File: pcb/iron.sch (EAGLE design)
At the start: 22 parts, among them IC1 AT24CS04-SOT23, IC2 TS507CLT, IC3 AD7995, IC4 ESDA6V1SC5, X1 LUMBERG_KLB_4

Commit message: reworked iron parts
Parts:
- C1: OC_DIGIKEY (none) -> 478-7926-1-ND; OC_MOUSER 710-885012207080 -> (none)
- C2: OC_DIGIKEY (none) -> 478-6209-1-ND; OC_MOUSER 710-885012207092 -> (none)
- R1: value 20k 0,1% -> 1k; OC_DIGIKEY P20KDBCT-ND -> P1.0KDBCT-ND
- R2: value 68k @25°C, 1%, ß=3985 K -> 1k @25°C, 1%, ß=3650 K; OC_DIGIKEY BC2555CT-ND -> P123687CT-ND
- R4: value 5,1M -> 4M7; OC_DIGIKEY (none) -> 311-4.70MHRCT-ND; OC_MOUSER 71-CRCW08055M10FKEA -> (none)
- R6: value 1k -> 100k; OC_DIGIKEY RMCF0603FT1K00CT-ND -> RMCF0603FT100KCT-ND
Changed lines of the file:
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@@
 <part name="X1" library="solderpi" library_urn="urn:adsk.eagle:library:1437534" deviceset="LUMBERG_KLB_4" device="" package3d_urn="urn:adsk.eagle:package:1437574/2"/>
 <part name="GND1" library="supply1" library_urn="urn:adsk.eagle:library:371" deviceset="GND" device=""/>
-<part name="R1" library="common" library_urn="urn:adsk.eagle:library:8241912" deviceset="R-EU" device="0603" package3d_urn="urn:adsk.eagle:package:8241925/3" value="20k 0,1%">
-<spice>
-<pinmapping spiceprefix="R">
-<pinmap gate="G$1" pin="1" pinorder="1"/>
-<pinmap gate="G$1" pin="2" pinorder="2"/>
-</pinmapping>
-</spice>
-<attribute name="OC_DIGIKEY" value="P20KDBCT-ND"/>
-</part>
-<part name="R2" library="common" library_urn="urn:adsk.eagle:library:8241912" deviceset="NTC" device="0603" package3d_urn="urn:adsk.eagle:package:8241925/3" value="68k @25°C, 1%, ß=3985 K">
-<attribute name="OC_DIGIKEY" value="BC2555CT-ND"/>
+<part name="R1" library="common" library_urn="urn:adsk.eagle:library:8241912" deviceset="R-EU" device="0603" package3d_urn="urn:adsk.eagle:package:8241925/3" value="1k">
+<spice>
+<pinmapping spiceprefix="R">
+<pinmap gate="G$1" pin="1" pinorder="1"/>
+<pinmap gate="G$1" pin="2" pinorder="2"/>
+</pinmapping>
+</spice>
+<attribute name="OC_DIGIKEY" value="P1.0KDBCT-ND"/>
+</part>
+<part name="R2" library="common" library_urn="urn:adsk.eagle:library:8241912" deviceset="NTC" device="0603" package3d_urn="urn:adsk.eagle:package:8241925/3" value="1k @25°C, 1%, ß=3650 K">
+<attribute name="OC_DIGIKEY" value="P123687CT-ND"/>
 </part>
 <part name="P+1" library="supply1" library_urn="urn:adsk.eagle:library:371" deviceset="+5V" device=""/>
@@
 <part name="GND4" library="supply1" library_urn="urn:adsk.eagle:library:371" deviceset="GND" device=""/>
 <part name="P+2" library="supply1" library_urn="urn:adsk.eagle:library:371" deviceset="+5V" device=""/>
-<part name="R4" library="common" library_urn="urn:adsk.eagle:library:8241912" deviceset="R-EU" device="0603" package3d_urn="urn:adsk.eagle:package:8241925/3" value="5,1M">
-<spice>
-<pinmapping spiceprefix="R">
-<pinmap gate="G$1" pin="1" pinorder="1"/>
-<pinmap gate="G$1" pin="2" pinorder="2"/>
-</pinmapping>
-</spice>
-<attribute name="OC_MOUSER" value="71-CRCW08055M10FKEA"/>
+<part name="R4" library="common" library_urn="urn:adsk.eagle:library:8241912" deviceset="R-EU" device="0603" package3d_urn="urn:adsk.eagle:package:8241925/3" value="4M7">
+<spice>
+<pinmapping spiceprefix="R">
+<pinmap gate="G$1" pin="1" pinorder="1"/>
+<pinmap gate="G$1" pin="2" pinorder="2"/>
+</pinmapping>
+</spice>
+<attribute name="OC_DIGIKEY" value="311-4.70MHRCT-ND"/>
 </part>
 <part name="R5" library="common" library_urn="urn:adsk.eagle:library:8241912" deviceset="R-EU" device="0603" package3d_urn="urn:adsk.eagle:package:8241925/3" value="1k">
@@
 <attribute name="OC_DIGIKEY" value=" RMCF0603FT1K00CT-ND"/>
 </part>
-<part name="R6" library="common" library_urn="urn:adsk.eagle:library:8241912" deviceset="R-EU" device="0603" package3d_urn="urn:adsk.eagle:package:8241925/3" value="1k">
-<spice>
-<pinmapping spiceprefix="R">
-<pinmap gate="G$1" pin="1" pinorder="1"/>
-<pinmap gate="G$1" pin="2" pinorder="2"/>
-</pinmapping>
-</spice>
-<attribute name="OC_DIGIKEY" value=" RMCF0603FT1K00CT-ND"/>
+<part name="R6" library="common" library_urn="urn:adsk.eagle:library:8241912" deviceset="R-EU" device="0603" package3d_urn="urn:adsk.eagle:package:8241925/3" value="100k">
+<spice>
+<pinmapping spiceprefix="R">
+<pinmap gate="G$1" pin="1" pinorder="1"/>
+<pinmap gate="G$1" pin="2" pinorder="2"/>
+</pinmapping>
+</spice>
+<attribute name="OC_DIGIKEY" value="RMCF0603FT100KCT-ND"/>
 </part>
 <part name="C1" library="common" library_urn="urn:adsk.eagle:library:8241912" deviceset="C-EU" device="0603" package3d_urn="urn:adsk.eagle:package:8241929/3" value="100pF">
@@
 </pinmapping>
 </spice>
-<attribute name="OC_MOUSER" value="710-885012207080"/>
+<attribute name="OC_DIGIKEY" value="478-7926-1-ND"/>
 </part>
 <part name="C2" library="common" library_urn="urn:adsk.eagle:library:8241912" deviceset="C-EU" device="0603" package3d_urn="urn:adsk.eagle:package:8241929/3" value="10nF">
@@
 </pinmapping>
 </spice>
-<attribute name="OC_MOUSER" value="710-885012207092 "/>
+<attribute name="OC_DIGIKEY" value="478-6209-1-ND"/>
 </part>
 <part name="P+3" library="supply1" library_urn="urn:adsk.eagle:library:371" deviceset="+5V" device=""/>
@@
 </instance>
 <instance part="R4" gate="G$1" x="22.86" y="66.04" smashed="yes" rot="R90">
-<attribute name="OC_MOUSER" x="22.86" y="66.04" size="1.778" layer="96" rot="R90" display="off"/>
+<attribute name="OC_DIGIKEY" x="22.86" y="66.04" size="1.778" layer="96" rot="R90" display="off"/>
 <attribute name="NAME" x="21.3614" y="62.23" size="1.778" layer="95" rot="R90"/>
 <attribute name="VALUE" x="26.162" y="62.23" size="1.778" layer="96" rot="R90"/>
@@
 </instance>
 <instance part="C1" gate="G$1" x="12.7" y="63.5" smashed="yes">
-<attribute name="OC_MOUSER" x="12.7" y="63.5" size="1.778" layer="96" display="off"/>
+<attribute name="OC_DIGIKEY" x="12.7" y="63.5" size="1.778" layer="96" display="off"/>
 <attribute name="NAME" x="14.224" y="63.881" size="1.778" layer="95"/>
 <attribute name="VALUE" x="14.224" y="58.801" size="1.778" layer="96"/>
 </instance>
 <instance part="C2" gate="G$1" x="60.96" y="111.76" smashed="yes">
-<attribute name="OC_MOUSER" x="60.96" y="111.76" size="1.778" layer="96" display="off"/>
+<attribute name="OC_DIGIKEY" x="60.96" y="111.76" size="1.778" layer="96" display="off"/>
 <attribute name="NAME" x="62.484" y="112.141" size="1.778" layer="95"/>
 <attribute name="VALUE" x="62.484" y="107.061" size="1.778" layer="96"/>

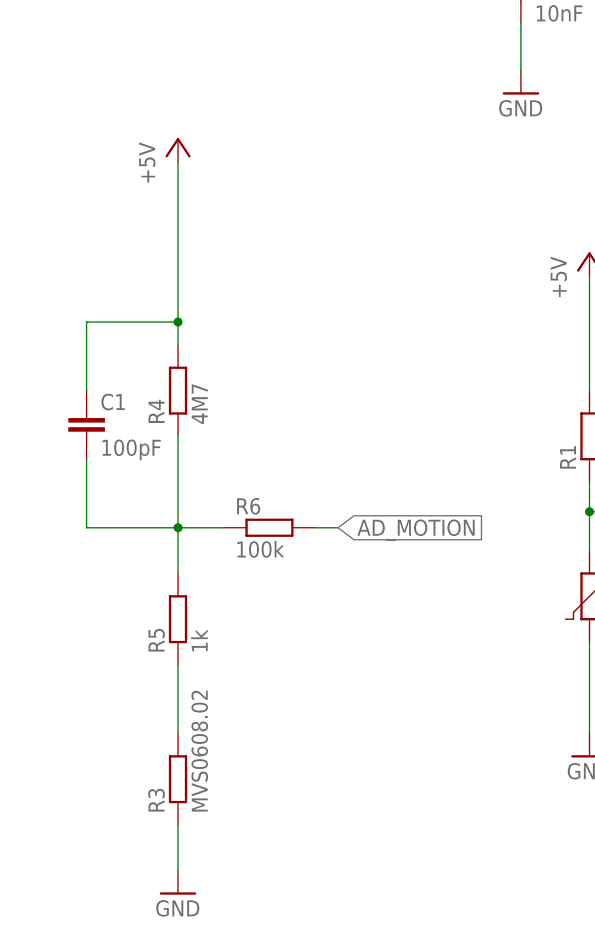
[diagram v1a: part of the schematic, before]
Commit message: shottky diode added to iron/tweezer
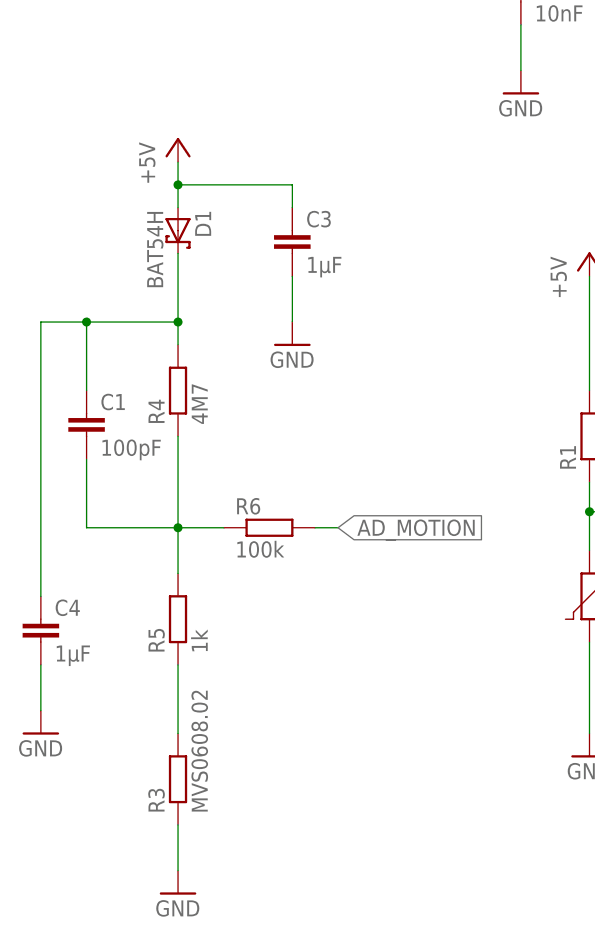
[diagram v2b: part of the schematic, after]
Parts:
- added C3, C4: 1µF, common:C-EU0603
- added D1: BAT54H, solderpi:BAT54H
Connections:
- new net N$1: C1.1, C4.1, D1.C, R4.2
- net +5V: now also C3.1, D1.A; no longer C1.1, R4.2
- net GND: now also C3.2, C4.2
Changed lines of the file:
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@@
 <attribute name="OC_DIGIKEY" value="YAG4498CT-ND"/>
 </part>
+<part name="D1" library="solderpi" library_urn="urn:adsk.eagle:library:1437534" deviceset="BAT54H" device="" package3d_urn="urn:adsk.eagle:package:1609183/2">
+<attribute name="OC_DIGIKEY" value="1727-3569-1-ND"/>
+</part>
+<part name="C3" library="common" library_urn="urn:adsk.eagle:library:8241912" deviceset="C-EU" device="0603" package3d_urn="urn:adsk.eagle:package:8241929/3" value="1µF">
+<spice>
+<pinmapping spiceprefix="C">
+<pinmap gate="G$1" pin="1" pinorder="1"/>
+<pinmap gate="G$1" pin="2" pinorder="2"/>
+</pinmapping>
+</spice>
+<attribute name="OC_DIGIKEY" value="1276-1034-1-ND"/>
+</part>
+<part name="GND11" library="supply1" library_urn="urn:adsk.eagle:library:371" deviceset="GND" device=""/>
+<part name="C4" library="common" library_urn="urn:adsk.eagle:library:8241912" deviceset="C-EU" device="0603" package3d_urn="urn:adsk.eagle:package:8241929/3" value="1µF">
+<spice>
+<pinmapping spiceprefix="C">
+<pinmap gate="G$1" pin="1" pinorder="1"/>
+<pinmap gate="G$1" pin="2" pinorder="2"/>
+</pinmapping>
+</spice>
+<attribute name="OC_DIGIKEY" value="1276-1034-1-ND"/>
+</part>
+<part name="GND12" library="supply1" library_urn="urn:adsk.eagle:library:371" deviceset="GND" device=""/>
 </parts>
 <sheets>
@@
 <attribute name="VALUE" x="112.522" y="102.87" size="1.778" layer="96" rot="R90"/>
 </instance>
+<instance part="D1" gate="G$1" x="22.86" y="83.82" smashed="yes" rot="R270">
+<attribute name="NAME" x="24.765" y="86.106" size="1.778" layer="95" rot="R270"/>
+<attribute name="VALUE" x="19.431" y="86.106" size="1.778" layer="96" rot="R270"/>
+<attribute name="OC_DIGIKEY" x="22.86" y="83.82" size="1.778" layer="96" rot="R270" display="off"/>
+</instance>
+<instance part="C3" gate="G$1" x="35.56" y="83.82" smashed="yes">
+<attribute name="OC_DIGIKEY" x="35.56" y="83.82" size="1.778" layer="96" display="off"/>
+<attribute name="NAME" x="37.084" y="84.201" size="1.778" layer="95"/>
+<attribute name="VALUE" x="37.084" y="79.121" size="1.778" layer="96"/>
+</instance>
+<instance part="GND11" gate="1" x="35.56" y="71.12" smashed="yes">
+<attribute name="VALUE" x="33.02" y="68.58" size="1.778" layer="96"/>
+</instance>
+<instance part="C4" gate="G$1" x="7.62" y="40.64" smashed="yes">
+<attribute name="OC_DIGIKEY" x="7.62" y="40.64" size="1.778" layer="96" display="off"/>
+<attribute name="NAME" x="9.144" y="41.021" size="1.778" layer="95"/>
+<attribute name="VALUE" x="9.144" y="35.941" size="1.778" layer="96"/>
+</instance>
+<instance part="GND12" gate="1" x="7.62" y="27.94" smashed="yes">
+<attribute name="VALUE" x="5.08" y="25.4" size="1.778" layer="96"/>
+</instance>
 </instances>
 <busses>
@@
 <wire x1="91.44" y1="104.14" x2="91.44" y2="106.68" width="0.1524" layer="91"/>
 </segment>
+<segment>
+<pinref part="GND11" gate="1" pin="GND"/>
+<pinref part="C3" gate="G$1" pin="2"/>
+<wire x1="35.56" y1="73.66" x2="35.56" y2="78.74" width="0.1524" layer="91"/>
+</segment>
+<segment>
+<pinref part="GND12" gate="1" pin="GND"/>
+<pinref part="C4" gate="G$1" pin="2"/>
+<wire x1="7.62" y1="30.48" x2="7.62" y2="35.56" width="0.1524" layer="91"/>
+</segment>
 </net>
 <net name="AD_COMP" class="0">
@@
 <wire x1="182.88" y1="45.72" x2="182.88" y2="50.8" width="0.1524" layer="91"/>
 <pinref part="P+2" gate="1" pin="+5V"/>
-</segment>
-<segment>
-<pinref part="C1" gate="G$1" pin="1"/>
-<wire x1="12.7" y1="66.04" x2="12.7" y2="73.66" width="0.1524" layer="91"/>
-<pinref part="R4" gate="G$1" pin="2"/>
-<wire x1="12.7" y1="73.66" x2="22.86" y2="73.66" width="0.1524" layer="91"/>
-<wire x1="22.86" y1="73.66" x2="22.86" y2="71.12" width="0.1524" layer="91"/>
-<pinref part="P+3" gate="1" pin="+5V"/>
-<wire x1="22.86" y1="73.66" x2="22.86" y2="91.44" width="0.1524" layer="91"/>
-<junction x="22.86" y="73.66"/>
 </segment>
 <segment>
@@
 <pinref part="P+6" gate="1" pin="+5V"/>
 <wire x1="91.44" y1="121.92" x2="91.44" y2="127" width="0.1524" layer="91"/>
+</segment>
+<segment>
+<pinref part="D1" gate="G$1" pin="A"/>
+<pinref part="P+3" gate="1" pin="+5V"/>
+<wire x1="22.86" y1="86.36" x2="22.86" y2="88.9" width="0.1524" layer="91"/>
+<pinref part="C3" gate="G$1" pin="1"/>
+<wire x1="22.86" y1="88.9" x2="22.86" y2="91.44" width="0.1524" layer="91"/>
+<wire x1="35.56" y1="86.36" x2="35.56" y2="88.9" width="0.1524" layer="91"/>
+<wire x1="35.56" y1="88.9" x2="22.86" y2="88.9" width="0.1524" layer="91"/>
+<junction x="22.86" y="88.9"/>
 </segment>
 </net>
@@
 </segment>
 </net>
+<net name="N$1" class="0">
+<segment>
+<pinref part="C1" gate="G$1" pin="1"/>
+<wire x1="12.7" y1="66.04" x2="12.7" y2="73.66" width="0.1524" layer="91"/>
+<pinref part="R4" gate="G$1" pin="2"/>
+<wire x1="12.7" y1="73.66" x2="22.86" y2="73.66" width="0.1524" layer="91"/>
+<wire x1="22.86" y1="73.66" x2="22.86" y2="71.12" width="0.1524" layer="91"/>
+<junction x="22.86" y="73.66"/>
+<pinref part="D1" gate="G$1" pin="C"/>
+<wire x1="22.86" y1="73.66" x2="22.86" y2="81.28" width="0.1524" layer="91"/>
+<pinref part="C4" gate="G$1" pin="1"/>
+<wire x1="7.62" y1="43.18" x2="7.62" y2="73.66" width="0.1524" layer="91"/>
+<wire x1="7.62" y1="73.66" x2="12.7" y2="73.66" width="0.1524" layer="91"/>
+<junction x="12.7" y="73.66"/>
+</segment>
+</net>

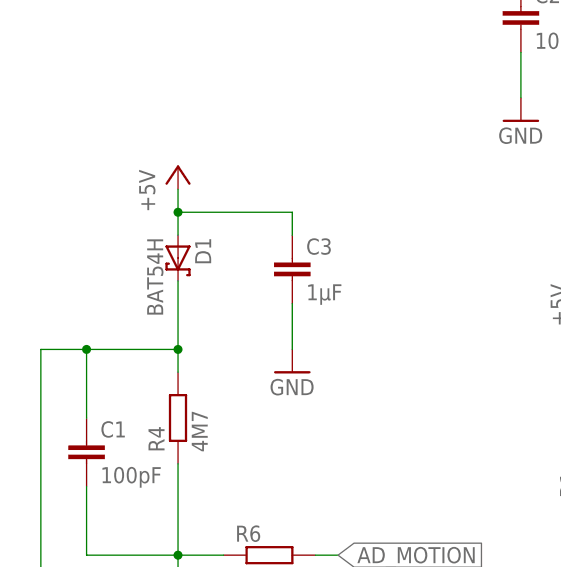
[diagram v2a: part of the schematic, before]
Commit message: iron tweezer updated
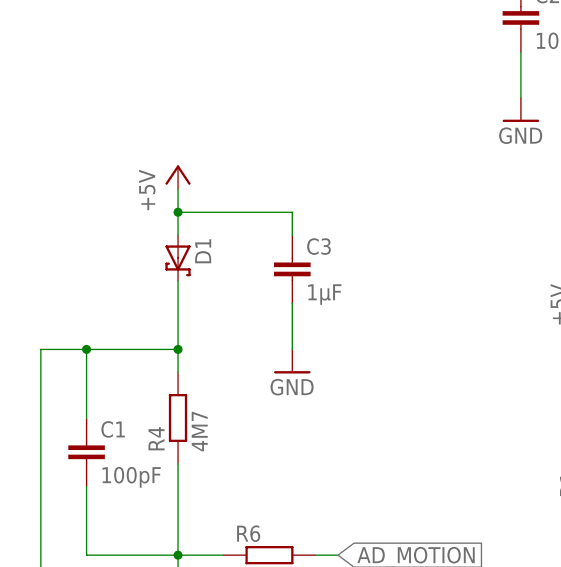
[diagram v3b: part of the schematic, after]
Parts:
- IC2: OC_DIGIKEY TS507CLT -> 497-6944-1-ND
- X1: OC_DIGIKEY (none) -> 486-3419-ND
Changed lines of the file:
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@@
 <parts>
 <part name="FRAME1" library="frames" library_urn="urn:adsk.eagle:library:229" deviceset="A4L-LOC" device=""/>
-<part name="X1" library="solderpi" library_urn="urn:adsk.eagle:library:1437534" deviceset="LUMBERG_KLB_4" device="" package3d_urn="urn:adsk.eagle:package:1437574/2"/>
+<part name="X1" library="solderpi" library_urn="urn:adsk.eagle:library:1437534" deviceset="LUMBERG_KLB_4" device="" package3d_urn="urn:adsk.eagle:package:1437574/2">
+<attribute name="OC_DIGIKEY" value="486-3419-ND"/>
+</part>
 <part name="GND1" library="supply1" library_urn="urn:adsk.eagle:library:371" deviceset="GND" device=""/>
 <part name="R1" library="common" library_urn="urn:adsk.eagle:library:8241912" deviceset="R-EU" device="0603" package3d_urn="urn:adsk.eagle:package:8241925/3" value="1k">
@@
 <part name="GND6" library="supply1" library_urn="urn:adsk.eagle:library:371" deviceset="GND" device=""/>
 <part name="IC2" library="solderpi" library_urn="urn:adsk.eagle:library:1437534" deviceset="TS507CLT" device="" package3d_urn="urn:adsk.eagle:package:1437676/7">
-<attribute name="OC_DIGIKEY" value="TS507CLT"/>
+<attribute name="OC_DIGIKEY" value="497-6944-1-ND"/>
 </part>
 <part name="GND8" library="supply1" library_urn="urn:adsk.eagle:library:371" deviceset="GND" device=""/>
@@
 <attribute name="NAME" x="22.86" y="153.67" size="1.778" layer="95"/>
 <attribute name="VALUE" x="22.86" y="143.51" size="1.778" layer="96"/>
+<attribute name="OC_DIGIKEY" x="25.4" y="149.86" size="1.778" layer="96" display="off"/>
 </instance>
 <instance part="GND1" gate="1" x="48.26" y="144.78" smashed="yes">
@@
 <instance part="D1" gate="G$1" x="22.86" y="83.82" smashed="yes" rot="R270">
 <attribute name="NAME" x="24.765" y="86.106" size="1.778" layer="95" rot="R270"/>
-<attribute name="VALUE" x="19.431" y="86.106" size="1.778" layer="96" rot="R270"/>
 <attribute name="OC_DIGIKEY" x="22.86" y="83.82" size="1.778" layer="96" rot="R270" display="off"/>
 </instance>
